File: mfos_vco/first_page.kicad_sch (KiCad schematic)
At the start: 44 parts, among them Q1 PN4391, Q1Ar1 2N3904, Q1Br1 2N3904, U1 OP275, U2 TL072, U3 SSM2210

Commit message: finished second page of schematic
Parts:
- added C_e10, C_e7, C_e8, C_e9: 1uf, Capacitor_SMD:C_0805_2012Metric_Pad1.18x1.45mm_HandSolder, symbol Device:C_Small
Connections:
- net +12V: now also C_e7.1, C_e9.1
- net -12V: now also C_e10.1, C_e8.1
- net GND: now also C_e10.2, C_e7.2, C_e8.2

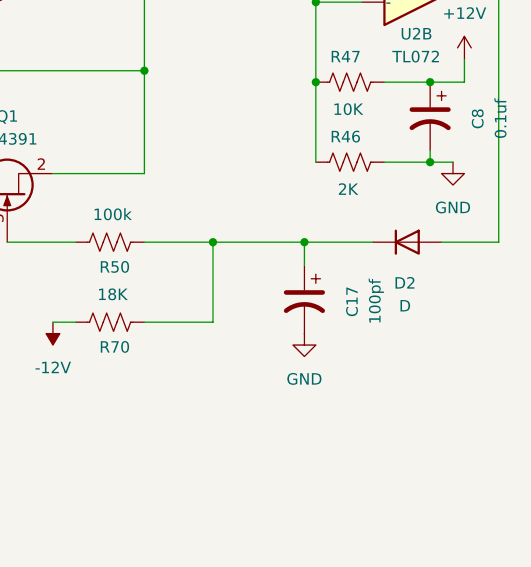
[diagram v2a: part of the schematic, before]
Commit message: added footprints
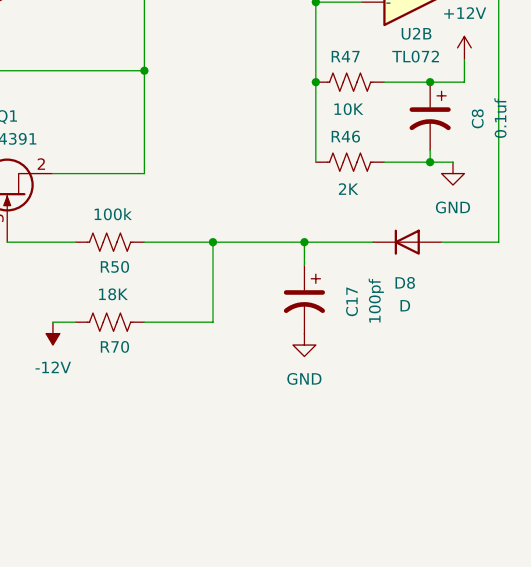
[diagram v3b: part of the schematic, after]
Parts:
- C17, C18, C19, C3, C5, C6, C8: footprint (none) -> Capacitor_THT:CP_Radial_Tantal_D4.5mm_P5.00mm
- D1: footprint (none) -> Diode_THT:D_T-1_P5.08mm_Horizontal
- D8: renamed from D2; footprint (none) -> Diode_THT:D_T-1_P5.08mm_Horizontal
- Q1: footprint (none) -> Package_TO_SOT_THT:TO-92L_Inline
- R10, R15, R17, R18, R19, R23, R24, R27, R28, R30, R31, R34, R42, R46, R47, R50, R56, R57, R65, R66, R69, R70, R71, R8, R9: footprint (none) -> custom_footprints:R_SMD_AND_THT
- R11, R16: footprint (none) -> Potentiometer_THT:Potentiometer_Bourns_3296W_Vertical
- U1, U2: footprint (none) -> Package_DIP:DIP-8_W7.62mm
- U3: footprint (none) -> Package_DIP:DIP-6_W7.62mm
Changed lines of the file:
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@@
 			)
 		)
-		(property "Footprint" ""
+		(property "Footprint" "Capacitor_THT:CP_Radial_Tantal_D4.5mm_P5.00mm"
 			(at 246.38 36.83 0)
 			(effects
@@
 			)
 		)
-		(property "Footprint" ""
+		(property "Footprint" "custom_footprints:R_SMD_AND_THT"
 			(at 164.846 123.444 90)
 			(effects
@@
 			)
 		)
-		(property "Footprint" ""
+		(property "Footprint" "Potentiometer_THT:Potentiometer_Bourns_3296W_Vertical"
 			(at 120.65 96.52 0)
 			(effects
@@
 			)
 		)
-		(property "Footprint" ""
+		(property "Footprint" "Potentiometer_THT:Potentiometer_Bourns_3296W_Vertical"
 			(at 160.02 77.47 0)
 			(effects
@@
 			)
 		)
-		(property "Footprint" ""
+		(property "Footprint" "Package_DIP:DIP-8_W7.62mm"
 			(at 273.05 77.47 0)
 			(effects
@@
 			)
 		)
-		(property "Footprint" ""
+		(property "Footprint" "custom_footprints:R_SMD_AND_THT"
 			(at 237.744 105.664 90)
 			(effects
@@
 			)
 		)
-		(property "Footprint" ""
+		(property "Footprint" "custom_footprints:R_SMD_AND_THT"
 			(at 243.586 44.704 90)
 			(effects
@@
 			)
 		)
-		(property "Footprint" ""
+		(property "Footprint" "custom_footprints:R_SMD_AND_THT"
 			(at 144.526 133.604 90)
 			(effects
@@
 			)
 		)
-		(property "Footprint" ""
+		(property "Footprint" "custom_footprints:R_SMD_AND_THT"
 			(at 27.686 57.404 90)
 			(effects
@@
 			)
 		)
-		(property "Footprint" ""
+		(property "Footprint" "Package_DIP:DIP-8_W7.62mm"
 			(at 200.66 43.18 0)
 			(effects
@@
 			)
 		)
-		(property "Footprint" ""
+		(property "Footprint" "Package_DIP:DIP-6_W7.62mm"
 			(at 140.97 96.52 0)
 			(effects
@@
 			)
 		)
-		(property "Footprint" ""
+		(property "Footprint" "custom_footprints:R_SMD_AND_THT"
 			(at 172.466 88.646 90)
 			(effects
@@
 			)
 		)
-		(property "Footprint" ""
+		(property "Footprint" "Capacitor_THT:CP_Radial_Tantal_D4.5mm_P5.00mm"
 			(at 273.05 92.71 0)
 			(effects
@@
 		(on_board yes)
 		(dnp no)
-		(property "Reference" "D2"
+		(property "Reference" "D8"
 			(at 270.256 111.252 0)
 			(effects
@@
 			)
 		)
-		(property "Footprint" ""
+		(property "Footprint" "Diode_THT:D_T-1_P5.08mm_Horizontal"
 			(at 270.51 106.68 0)
 			(effects
@@
 			(project "mfos_vco"
 				(path "/db27d43e-bcf4-48a8-8785-18123cee165a/da218509-bd5d-4011-8fb3-339b9a173cb1"
-					(reference "D2")
+					(reference "D8")
 					(unit 1)
 				)
@@
 			)
 		)
-		(property "Footprint" ""
+		(property "Footprint" "Capacitor_THT:CP_Radial_Tantal_D4.5mm_P5.00mm"
 			(at 96.52 133.35 0)
 			(effects
@@
 			)
 		)
-		(property "Footprint" ""
+		(property "Footprint" "custom_footprints:R_SMD_AND_THT"
 			(at 263.906 89.916 90)
 			(effects
@@
 			)
 		)
-		(property "Footprint" ""
+		(property "Footprint" "custom_footprints:R_SMD_AND_THT"
 			(at 139.954 142.494 90)
 			(effects
@@
 			)
 		)
-		(property "Footprint" ""
+		(property "Footprint" "custom_footprints:R_SMD_AND_THT"
 			(at 75.184 98.044 90)
 			(effects
@@
 			)
 		)
-		(property "Footprint" ""
+		(property "Footprint" "Package_DIP:DIP-8_W7.62mm"
 			(at 229.87 74.93 0)
 			(effects
@@
 			)
 		)
-		(property "Footprint" ""
+		(property "Footprint" "custom_footprints:R_SMD_AND_THT"
 			(at 27.686 70.104 90)
 			(effects
@@
 			)
 		)
-		(property "Footprint" ""
+		(property "Footprint" "custom_footprints:R_SMD_AND_THT"
 			(at 237.744 114.554 90)
 			(effects
@@
 			)
 		)
-		(property "Footprint" ""
+		(property "Footprint" "custom_footprints:R_SMD_AND_THT"
 			(at 75.184 139.954 90)
 			(effects
@@
 			)
 		)
-		(property "Footprint" ""
+		(property "Footprint" "Package_DIP:DIP-8_W7.62mm"
 			(at 186.69 43.18 0)
 			(effects
@@
 			)
 		)
-		(property "Footprint" ""
+		(property "Footprint" "custom_footprints:R_SMD_AND_THT"
 			(at 119.634 111.506 90)
 			(effects
@@
 			)
 		)
-		(property "Footprint" ""
+		(property "Footprint" "custom_footprints:R_SMD_AND_THT"
 			(at 263.906 98.806 90)
 			(effects
@@
 			)
 		)
-		(property "Footprint" ""
+		(property "Footprint" "Package_DIP:DIP-6_W7.62mm"
 			(at 160.02 96.52 0)
 			(effects
@@
 			)
 		)
-		(property "Footprint" ""
+		(property "Footprint" "custom_footprints:R_SMD_AND_THT"
 			(at 75.184 123.444 90)
 			(effects
@@
 			)
 		)
-		(property "Footprint" ""
+		(property "Footprint" "Capacitor_THT:CP_Radial_Tantal_D4.5mm_P5.00mm"
 			(at 259.08 113.03 0)
 			(effects
@@
 			)
 		)
-		(property "Footprint" ""
+		(property "Footprint" "Package_DIP:DIP-8_W7.62mm"
 			(at 182.88 107.95 0)
 			(effects
@@
 			)
 		)
-		(property "Footprint" ""
+		(property "Footprint" "custom_footprints:R_SMD_AND_THT"
 			(at 251.206 75.946 90)
 			(effects
@@
 			)
 		)
-		(property "Footprint" ""
+		(property "Footprint" "custom_footprints:R_SMD_AND_THT"
 			(at 147.066 78.486 90)
 			(effects
@@
 			)
 		)
-		(property "Footprint" ""
+		(property "Footprint" "custom_footprints:R_SMD_AND_THT"
 			(at 75.184 131.064 90)
 			(effects
@@
 			)
 		)
-		(property "Footprint" ""
+		(property "Footprint" "custom_footprints:R_SMD_AND_THT"
 			(at 255.016 37.846 90)
 			(effects
@@
 			)
 		)
-		(property "Footprint" ""
+		(property "Footprint" "Diode_THT:D_T-1_P5.08mm_Horizontal"
 			(at 135.89 77.47 0)
 			(effects
@@
 			)
 		)
-		(property "Footprint" ""
+		(property "Footprint" "custom_footprints:R_SMD_AND_THT"
 			(at 75.184 115.824 90)
 			(effects
@@
 			)
 		)
-		(property "Footprint" ""
+		(property "Footprint" "Capacitor_THT:CP_Radial_Tantal_D4.5mm_P5.00mm"
 			(at 215.9 87.63 0)
 			(effects
@@
 			)
 		)
-		(property "Footprint" ""
+		(property "Footprint" "custom_footprints:R_SMD_AND_THT"
 			(at 94.234 70.104 90)
 			(effects
@@
 			)
 		)
-		(property "Footprint" ""
+		(property "Footprint" "Package_TO_SOT_THT:TO-92L_Inline"
 			(at 223.52 96.52 0)
 			(effects
@@
 			)
 		)
-		(property "Footprint" ""
+		(property "Footprint" "Package_DIP:DIP-8_W7.62mm"
 			(at 95.25 88.9 0)
 			(effects
@@
 			)
 		)
-		(property "Footprint" ""
+		(property "Footprint" "Capacitor_THT:CP_Radial_Tantal_D4.5mm_P5.00mm"
 			(at 271.78 59.69 0)
 			(effects
@@
 			)
 		)
-		(property "Footprint" ""
+		(property "Footprint" "custom_footprints:R_SMD_AND_THT"
 			(at 75.184 106.934 90)
 			(effects
@@
 			)
 		)
-		(property "Footprint" ""
+		(property "Footprint" "custom_footprints:R_SMD_AND_THT"
 			(at 94.234 57.404 90)
 			(effects
@@
 			)
 		)
-		(property "Footprint" ""
+		(property "Footprint" "Capacitor_THT:CP_Radial_Tantal_D4.5mm_P5.00mm"
 			(at 186.69 128.27 0)
 			(effects
@@
 			)
 		)
-		(property "Footprint" ""
+		(property "Footprint" "custom_footprints:R_SMD_AND_THT"
 			(at 96.774 118.364 90)
 			(effects
@@
 			)
 		)
-		(property "Footprint" ""
+		(property "Footprint" "custom_footprints:R_SMD_AND_THT"
 			(at 271.526 69.596 90)
 			(effects

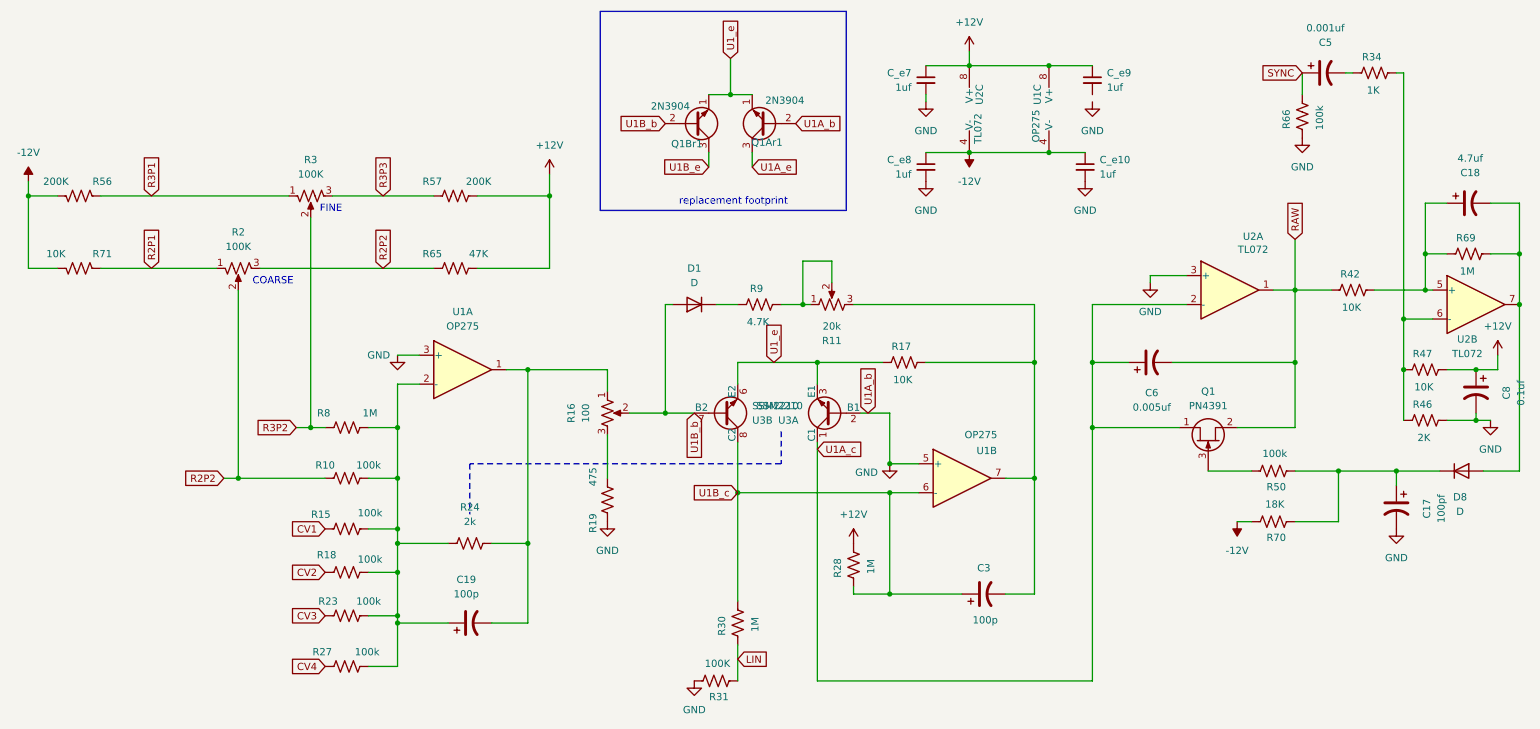
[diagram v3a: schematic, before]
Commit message: Finished placing components. Added a reference pic and footprint for the original design
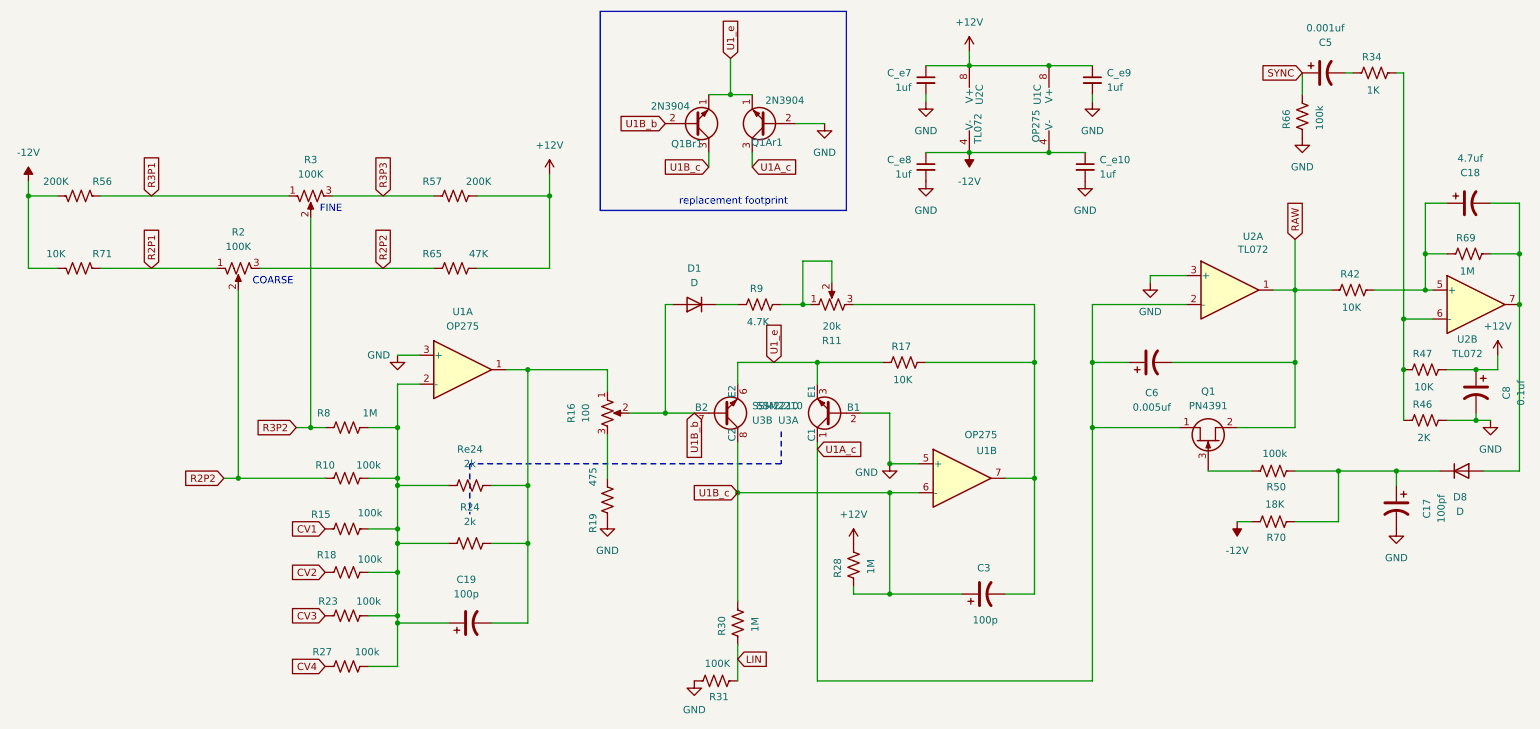
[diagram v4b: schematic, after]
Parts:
- added Re24: 2k, Resistor_THT:R_Axial_DIN0516_L15.5mm_D5.0mm_P20.32mm_Horizontal, symbol Device:R_US
- C17, C18, C19, C3, C5, C6, C8: footprint Capacitor_THT:CP_Radial_Tantal_D4.5mm_P5.00mm -> custom_footprints:cp_p5.0
- U3: footprint Package_DIP:DIP-6_W7.62mm -> Package_DIP:DIP-8_W7.62mm
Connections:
- net U1A_e is gone; now on net U1A_c: Q1Ar1.3 (C)
- net U1B_e is gone; now on net U1B_c: Q1Br1.3 (C)
- net GND: now also C_e9.2
- net at C19.2, R16.1, R24.2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: now also Re24.2
- net at C19.1, R10.2, R15.2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: now also Re24.1
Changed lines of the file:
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@@
 	)
 	(junction
+		(at 83.82 109.22)
+		(diameter 0)
+		(color 0 0 0 0)
+	)
+	(junction
 		(at 259.08 106.68)
 		(diameter 0)
@@
 	)
 	(junction
+		(at 106.68 109.22)
+		(diameter 0)
+		(color 0 0 0 0)
+	)
+	(junction
 		(at 273.05 97.79)
 		(diameter 0)
@@
 	(wire
 		(pts
+			(xy 83.82 109.22) (xy 92.71 109.22)
+		)
+		(stroke
+			(width 0)
+			(type default)
+		)
+	)
+	(wire
+		(pts
 			(xy 130.81 77.47) (xy 132.08 77.47)
 		)
@@
 	(wire
 		(pts
-			(xy 83.82 107.95) (xy 83.82 116.84)
+			(xy 83.82 107.95) (xy 83.82 109.22)
+		)
+		(stroke
+			(width 0)
+			(type default)
+		)
+	)
+	(wire
+		(pts
+			(xy 205.74 40.64) (xy 205.74 41.91)
 		)
 		(stroke
@@
 	(wire
 		(pts
+			(xy 153.67 45.72) (xy 158.75 45.72)
+		)
+		(stroke
+			(width 0)
+			(type default)
+		)
+	)
+	(wire
+		(pts
 			(xy 184.15 33.02) (xy 184.15 35.56)
 		)
@@
 	(wire
 		(pts
+			(xy 106.68 109.22) (xy 106.68 119.38)
+		)
+		(stroke
+			(width 0)
+			(type default)
+		)
+	)
+	(wire
+		(pts
 			(xy 83.82 99.06) (xy 83.82 107.95)
 		)
@@
 	(wire
 		(pts
+			(xy 83.82 109.22) (xy 83.82 116.84)
+		)
+		(stroke
+			(width 0)
+			(type default)
+		)
+	)
+	(wire
+		(pts
 			(xy 157.48 87.63) (xy 168.91 87.63)
 		)
@@
 	(wire
 		(pts
+			(xy 100.33 109.22) (xy 106.68 109.22)
+		)
+		(stroke
+			(width 0)
+			(type default)
+		)
+	)
+	(wire
+		(pts
 			(xy 259.08 106.68) (xy 266.7 106.68)
 		)
@@
 	(wire
 		(pts
-			(xy 106.68 88.9) (xy 106.68 119.38)
+			(xy 106.68 88.9) (xy 106.68 109.22)
 		)
 		(stroke
@@
 		)
 	)
-	(global_label "U1A_b"
-		(shape input)
-		(at 166.37 96.52 90)
-		(fields_autoplaced yes)
-		(effects
-			(font
-				(size 1.27 1.27)
-			)
-			(justify left)
-		)
-		(property "Intersheetrefs" "${INTERSHEET_REFS}"
-			(at 166.37 87.7896 90)
-			(effects
-				(font
-					(size 1.27 1.27)
-				)
-				(justify left)
-				(hide yes)
-			)
-		)
-	)
-	(global_label "U1B_e"
+	(global_label "U1B_c"
 		(shape input)
 		(at 138.43 53.34 180)
@@
 		)
 	)
-	(global_label "U1A_e"
+	(global_label "U1A_c"
 		(shape input)
 		(at 146.05 53.34 0)
@@
 		)
 	)
-	(global_label "U1A_b"
-		(shape input)
-		(at 153.67 45.72 0)
-		(fields_autoplaced yes)
-		(effects
-			(font
-				(size 1.27 1.27)
-			)
-			(justify left)
-		)
-		(property "Intersheetrefs" "${INTERSHEET_REFS}"
-			(at 162.4004 45.72 0)
-			(effects
-				(font
-					(size 1.27 1.27)
-				)
-				(justify left)
-				(hide yes)
-			)
-		)
-	)
 	(global_label "R3P1"
 		(shape input)
@@
 			)
 		)
-		(property "Footprint" "Capacitor_THT:CP_Radial_Tantal_D4.5mm_P5.00mm"
+		(property "Footprint" "custom_footprints:cp_p5.0"
 			(at 246.38 36.83 0)
 			(effects
@@
 	)
 	(symbol
+		(lib_id "Device:R_US")
+		(at 96.52 109.22 90)
+		(unit 1)
+		(exclude_from_sim no)
+		(in_bom yes)
+		(on_board yes)
+		(dnp no)
+		(fields_autoplaced yes)
+		(property "Reference" "Re24"
+			(at 96.52 102.87 90)
+			(effects
+				(font
+					(size 1.27 1.27)
+				)
+			)
+		)
+		(property "Value" "2k"
+			(at 96.52 105.41 90)
+			(effects
+				(font
+					(size 1.27 1.27)
+				)
+			)
+		)
+		(property "Footprint" "Resistor_THT:R_Axial_DIN0516_L15.5mm_D5.0mm_P20.32mm_Horizontal"
+			(at 96.774 108.204 90)
+			(effects
+				(font
+					(size 1.27 1.27)
+				)
+				(hide yes)
+			)
+		)
+		(property "Datasheet" "~"
+			(at 96.52 109.22 0)
+			(effects
+				(font
+					(size 1.27 1.27)
+				)
+				(hide yes)
+			)
+		)
+		(property "Description" "Resistor, US symbol"
+			(at 96.52 109.22 0)
+			(effects
+				(font
+					(size 1.27 1.27)
+				)
+				(hide yes)
+			)
+		)
+		(pin "1"
+		)
+		(pin "2"
+		)
+		(instances
+			(project "mfos_vco"
+				(path "/db27d43e-bcf4-48a8-8785-18123cee165a/da218509-bd5d-4011-8fb3-339b9a173cb1"
+					(reference "Re24")
+					(unit 1)
+				)
+			)
+		)
+	)
+	(symbol
 		(lib_id "Amplifier_Operational:TL072")
 		(at 273.05 77.47 0)
@@
 			)
 		)
-		(property "Footprint" "Package_DIP:DIP-6_W7.62mm"
+		(property "Footprint" "Package_DIP:DIP-8_W7.62mm"
 			(at 140.97 96.52 0)
 			(effects
@@
 			)
 		)
-		(property "Footprint" "Capacitor_THT:CP_Radial_Tantal_D4.5mm_P5.00mm"
+		(property "Footprint" "custom_footprints:cp_p5.0"
 			(at 273.05 92.71 0)
 			(effects
@@
 			)
 		)
-		(property "Footprint" "Capacitor_THT:CP_Radial_Tantal_D4.5mm_P5.00mm"
+		(property "Footprint" "custom_footprints:cp_p5.0"
 			(at 96.52 133.35 0)
 			(effects
@@
 			)
 		)
-		(property "Footprint" "Package_DIP:DIP-6_W7.62mm"
+		(property "Footprint" "Package_DIP:DIP-8_W7.62mm"
 			(at 160.02 96.52 0)
 			(effects
@@
 			)
 		)
-		(property "Footprint" "Capacitor_THT:CP_Radial_Tantal_D4.5mm_P5.00mm"
+		(property "Footprint" "custom_footprints:cp_p5.0"
 			(at 259.08 113.03 0)
 			(effects
@@
 	)
 	(symbol
+		(lib_id "power:GND")
+		(at 158.75 45.72 0)
+		(unit 1)
+		(exclude_from_sim no)
+		(in_bom yes)
+		(on_board yes)
+		(dnp no)
+		(fields_autoplaced yes)
+		(property "Reference" "#PWR051"
+			(at 158.75 52.07 0)
+			(effects
+				(font
+					(size 1.27 1.27)
+				)
+				(hide yes)
+			)
+		)
+		(property "Value" "GND"
+			(at 158.75 50.8 0)
+			(effects
+				(font
+					(size 1.27 1.27)
+				)
+			)
+		)
+		(property "Footprint" ""
+			(at 158.75 45.72 0)
+			(effects
+				(font
+					(size 1.27 1.27)
+				)
+				(hide yes)
+			)
+		)
+		(property "Datasheet" ""
+			(at 158.75 45.72 0)
+			(effects
+				(font
+					(size 1.27 1.27)
+				)
+				(hide yes)
+			)
+		)
+		(property "Description" "Power symbol creates a global label with name \"GND\" , ground"
+			(at 158.75 45.72 0)
+			(effects
+				(font
+					(size 1.27 1.27)
+				)
+				(hide yes)
+			)
+		)
+		(pin "1"
+		)
+		(instances
+			(project "mfos_vco"
+				(path "/db27d43e-bcf4-48a8-8785-18123cee165a/da218509-bd5d-4011-8fb3-339b9a173cb1"
+					(reference "#PWR051")
+					(unit 1)
+				)
+			)
+		)
+	)
+	(symbol
 		(lib_id "Device:R_US")
 		(at 74.93 132.08 90)
@@
 			)
 		)
-		(property "Footprint" "Capacitor_THT:CP_Radial_Tantal_D4.5mm_P5.00mm"
+		(property "Footprint" "custom_footprints:cp_p5.0"
 			(at 215.9 87.63 0)
 			(effects
@@
 			)
 		)
-		(property "Footprint" "Capacitor_THT:CP_Radial_Tantal_D4.5mm_P5.00mm"
+		(property "Footprint" "custom_footprints:cp_p5.0"
 			(at 271.78 59.69 0)
 			(effects
@@
 			)
 		)
-		(property "Footprint" "Capacitor_THT:CP_Radial_Tantal_D4.5mm_P5.00mm"
+		(property "Footprint" "custom_footprints:cp_p5.0"
 			(at 186.69 128.27 0)
 			(effects
